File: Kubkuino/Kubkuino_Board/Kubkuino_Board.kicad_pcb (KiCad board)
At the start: 2 copper layers, 55.1 x 36.3 mm, 35 parts, among them J1 Piezo, J2 ICSP, J3 I2C, J6 AC/DC In (12V), J7 Bluetooth, J8 Button, U1 ATmega328P-AU, U2 LM7805_TO220, Y1 Crystal

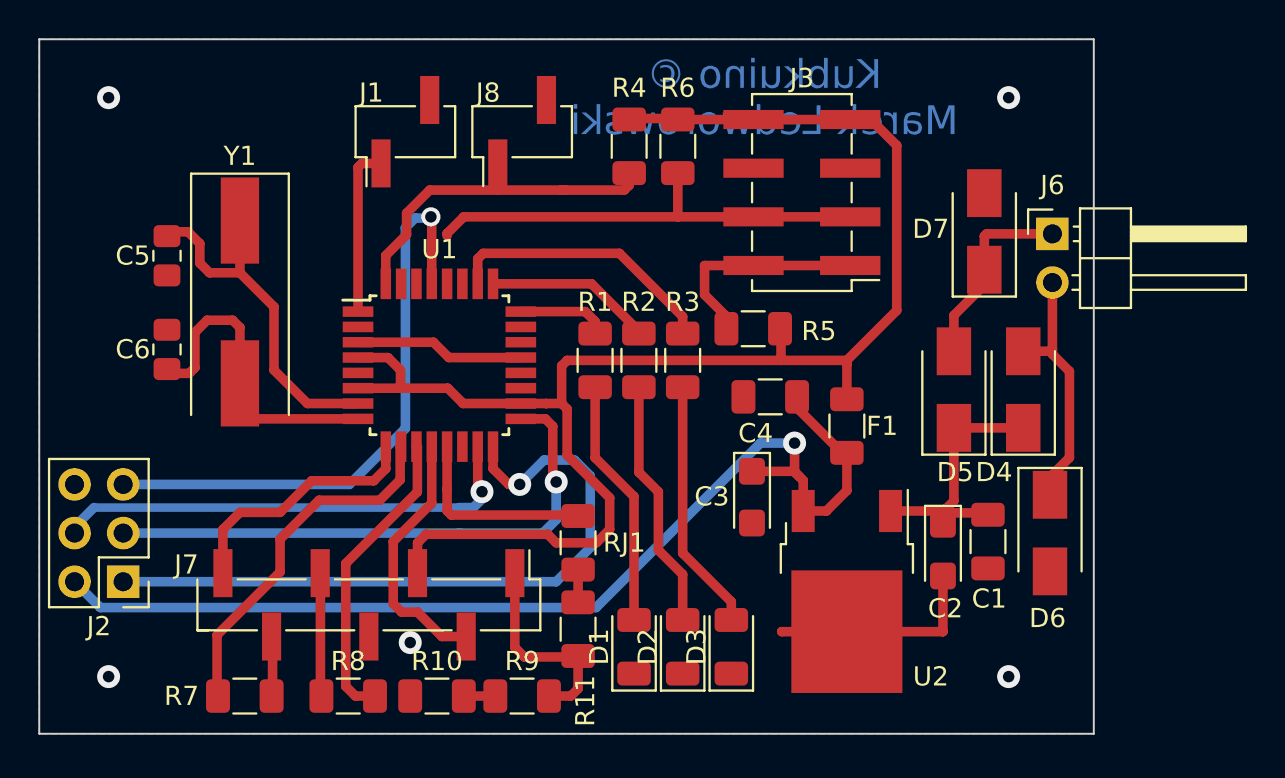
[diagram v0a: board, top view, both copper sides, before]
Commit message: Board optimization
Smaller board (couple of millimeters shorter)
Removed ICSP header
Added pads for programming
Changed rectifying section: DF08S (in schematic: DF08M, for THT change pads to through-hole)
Added missing resistor on reset line
No connections from before the fuse
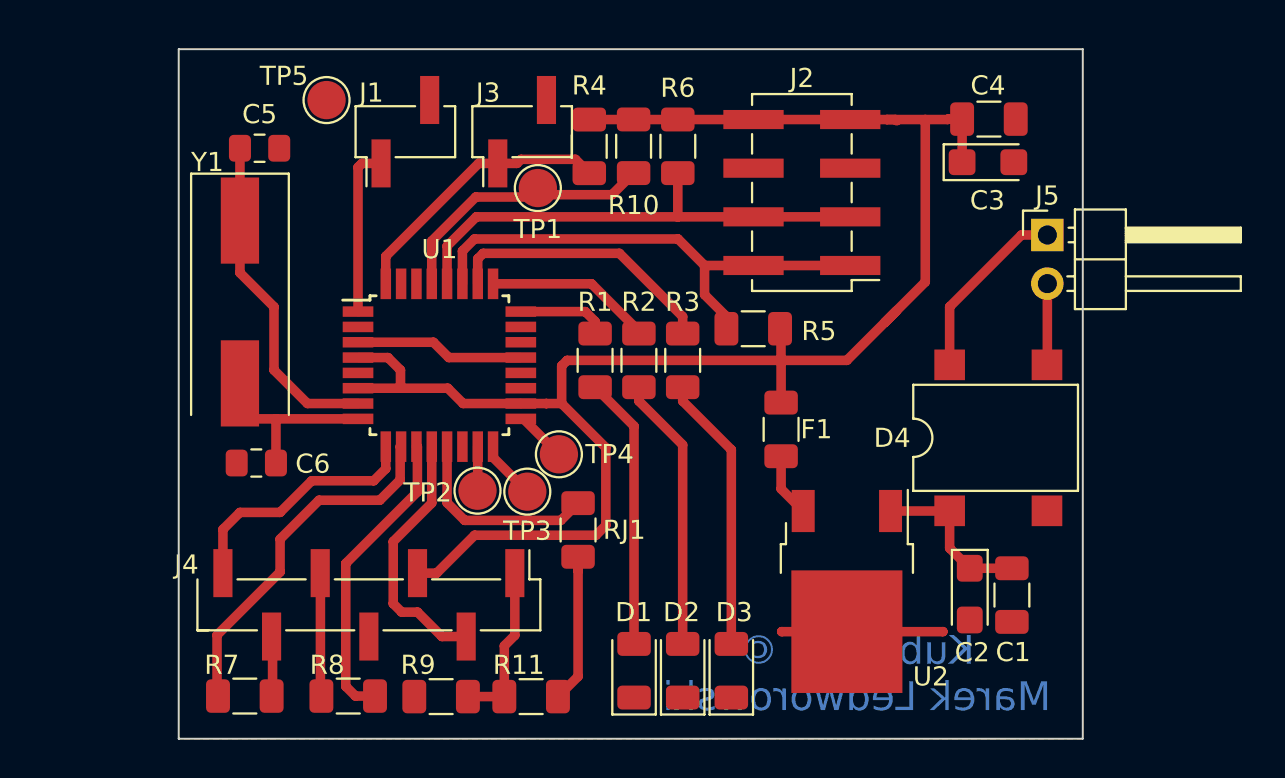
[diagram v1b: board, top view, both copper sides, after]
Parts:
- removed D5, D6, D7: 1N4007, Diode_SMD:D_SMA
- removed the J2 at (54.1, 49.4)
- added TP1: RESET, TestPoint:TestPoint_Pad_D2.0mm, F.Cu at (75.8, 28.9)
- added TP2: MOSI, TestPoint:TestPoint_Pad_D2.0mm, F.Cu at (72.6, 44.6)
- added TP3: MISO, TestPoint:TestPoint_Pad_D2.0mm, F.Cu at (75.2, 44.7)
- added TP4: SCK, TestPoint:TestPoint_Pad_D2.0mm, F.Cu at (76.8, 42.8)
- added TP5: GND, TestPoint:TestPoint_Pad_D2.0mm, F.Cu at (64.7, 24.3)
- D4: value 1N4007 -> DF08M; footprint Diode_SMD:D_SMA -> Diode_THT:Diode_Bridge_DIP-4_W7.62mm_P5.08mm
- R10, R9: value 4k7 -> 10k
- moved R10 30.5 mm to (80.8, 26.7), turned to 270 degrees
- moved C3 21.4 mm to (99.2, 27.5), turned to 0 degrees
- moved C4 18.5 mm to (99.3, 25.2), turned to 0 degrees
- moved C6 7.55 mm to (61.1, 43.2), turned to 180 degrees
- moved C5 7.41 mm to (61.2, 26.8), turned to 0 degrees
- moved D4 7.40 mm to (97.2, 45.7)
- moved R11 4.29 mm to (75.4, 55.4), turned to 180 degrees
- moved R9 4.23 mm to (70.7, 55.4)
- moved F1 3.44 mm to (88.5, 41.5)
- moved C1 3.06 mm to (100.5, 50.1)
- moved C2 2.69 mm to (98.3, 50.0)
- moved R4 2.08 mm to (78.4, 26.7), turned to 270 degrees
- moved D1 1.25 mm to (80.8, 54.0)
- moved D2 1.25 mm to (83.3, 54.0)
- moved D3 1.25 mm to (85.9, 54.0)
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- renumbered J3 to J2, J8 to J3, J7 to J4, J6 to J5
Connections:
- C3 pad 1: 5V_unfused -> 5V
- C4 pad 1: 5V_unfused -> 5V
- D4 pad 2: Net-(D4-Pad2) -> GND
- F1 pad 2: 5V_unfused -> Net-(F1-Pad2)
- J5 pad 1: Net-(D5-Pad2) -> Net-(D4-Pad4)
- J5 pad 2: Net-(D4-Pad2) -> Net-(D4-Pad3)
- R10 pad 1: GND -> 5V
- R10 pad 2: Net-(R10-Pad2) -> Reset
- R4 pad 1: Button -> 5V
- R4 pad 2: 5V -> Button
- R9 pad 1: Net-(R10-Pad2) -> GND
- U1 pad 15: Net-(J2-Pad4) -> /MOSI
- U1 pad 16: Net-(J2-Pad1) -> /MISO
- U1 pad 17: Net-(J2-Pad3) -> /SCK
- U1 pad 27: (no net) -> SDA
- U1 pad 28: (no net) -> SCL
- U2 pad 3: 5V_unfused -> Net-(F1-Pad2)
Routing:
- net 5V_unfused: track 56.7 -> 0.00 mm, vias 1 -> 0
- net Net-(J2-Pad1): track 36.3 -> 0.00 mm, vias 1 -> 0
- net Net-(J2-Pad3): track 29.7 -> 0.00 mm, vias 1 -> 0
- net Net-(J2-Pad4): track 25.0 -> 0.00 mm, vias 1 -> 0
- net Reset: track 31.5 -> 14.5 mm, vias 1 -> 0
- net SDA: track 11.4 -> 26.5 mm
- net Net-(D4-Pad2): track 13.5 -> 0.00 mm
- net Net-(D5-Pad2): track 10.8 -> 0.00 mm
- net 5V: track 82.3 -> 92.5 mm
- net Net-(D4-Pad4): track 0.00 -> 9.68 mm
- net xtal2: track 17.9 -> 9.40 mm
- net Net-(R11-Pad1): track 1.61 -> 7.74 mm
- net Net-(C1-Pad1): track 13.9 -> 8.72 mm
- net Net-(D4-Pad3): track 0.00 -> 4.25 mm
- net Button: track 18.6 -> 14.5 mm
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- removed copper zone on B.Cu, net GND
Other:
- board size 55.1 x 36.3 mm -> 47.2 x 36 mm
